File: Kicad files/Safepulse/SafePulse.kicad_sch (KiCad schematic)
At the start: 87 parts, among them IC1 S-35770E01I-K8T2U, J1 Conn_01x03_Male, J2 4208, Q1 FQT7N10L, Q2 BC846A, Q3 MMBT3906, Q4 MMBT3906, U1 TS4061AILT-1.25, U2 74HC14, U3 TLV27L1DBVT, U33 MAX9910EXK+T, U4 CD14538BM

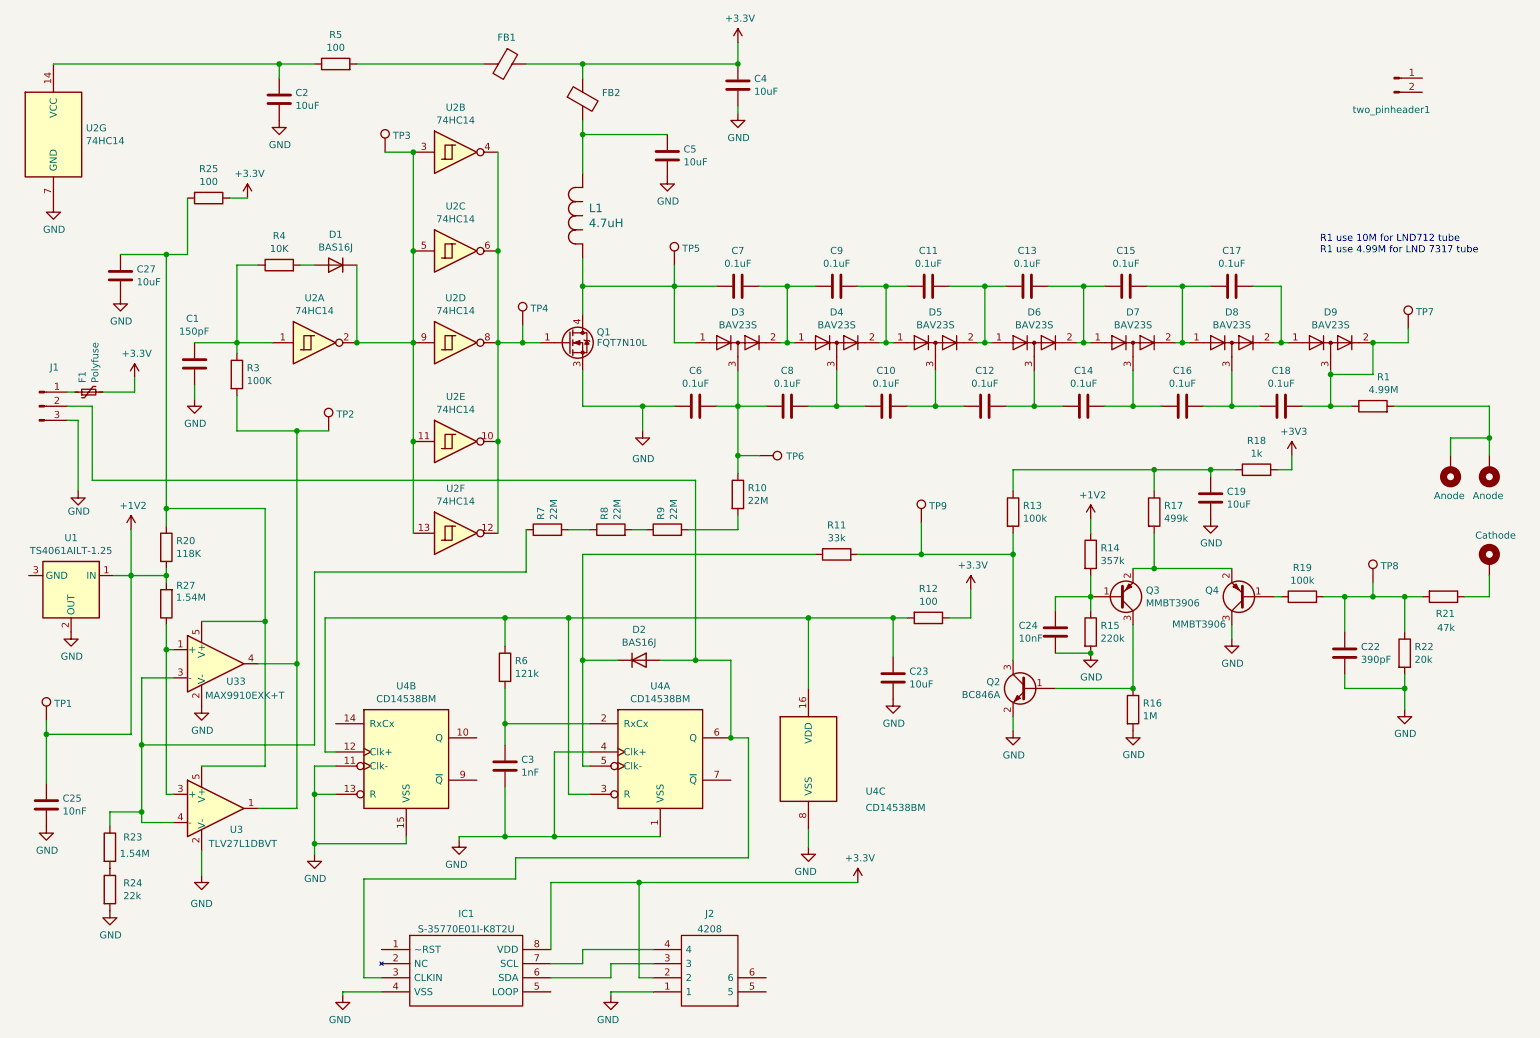
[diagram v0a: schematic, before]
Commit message: Updated C22 and R22 according to Joseph tests
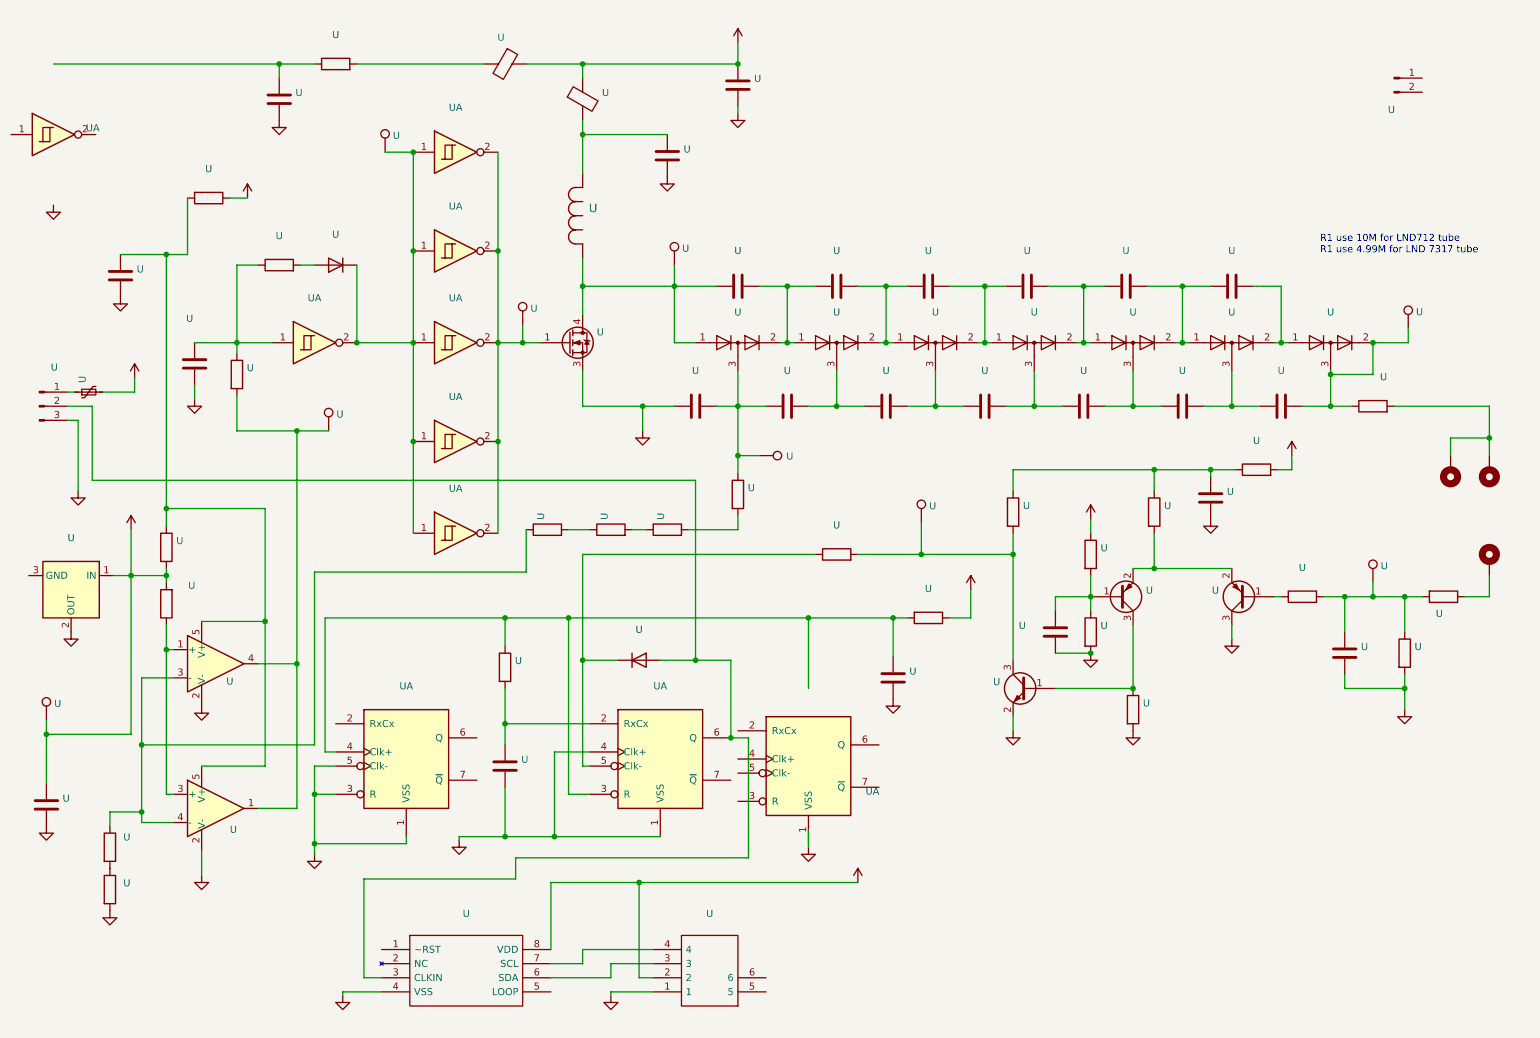
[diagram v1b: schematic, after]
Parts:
- U: renamed from U2; value 74HC14 -> (none); footprint Package_SO:SOIC-14_3.9x8.7mm_P1.27mm -> (none)
- U: renamed from D4; value BAV23S -> (none); footprint Package_TO_SOT_SMD:SOT-23 -> (none)
- U: renamed from D5; value BAV23S -> (none); footprint Package_TO_SOT_SMD:SOT-23 -> (none)
- U: renamed from D6; value BAV23S -> (none); footprint Package_TO_SOT_SMD:SOT-23 -> (none)
- U: renamed from D7; value BAV23S -> (none); footprint Package_TO_SOT_SMD:SOT-23 -> (none)
- U: renamed from D8; value BAV23S -> (none); footprint Package_TO_SOT_SMD:SOT-23 -> (none)
- U: renamed from D3; value BAV23S -> (none); footprint Package_TO_SOT_SMD:SOT-23 -> (none)
- U: renamed from D9; value BAV23S -> (none); footprint Package_TO_SOT_SMD:SOT-23 -> (none)
- U: renamed from C7; value 0.1uF -> (none); footprint Capacitor_SMD:C_0805_2012Metric -> (none)
- U: renamed from L1; value 4.7uH -> (none); footprint Inductor_SMD:L_Taiyo-Yuden_MD-4040 -> (none)
- U: renamed from R6; value 121k -> (none); footprint Resistor_SMD:R_0805_2012Metric -> (none)
- U: renamed from C5; value 10uF -> (none); footprint Capacitor_SMD:C_0805_2012Metric -> (none)
- U: renamed from R10; value 22M -> (none); footprint Resistor_SMD:R_0805_2012Metric -> (none)
- U: renamed from R9; value 22M -> (none); footprint Resistor_SMD:R_0805_2012Metric -> (none)
- U: renamed from R8; value 22M -> (none); footprint Resistor_SMD:R_0805_2012Metric -> (none)
- U: renamed from R7; value 22M -> (none); footprint Resistor_SMD:R_0805_2012Metric -> (none)
- U: renamed from R23; value 1.54M -> (none); footprint Resistor_SMD:R_0805_2012Metric -> (none)
- U: renamed from U4; value CD14538BM -> (none); footprint Package_SO:SOIC-16_3.9x9.9mm_P1.27mm -> (none)
- U: renamed from C3; value 1nF -> (none); footprint Capacitor_SMD:C_0805_2012Metric -> (none)
- U: renamed from FB1; value 74279220321 -> (none); footprint Resistor_SMD:R_0805_2012Metric -> (none)
- U: renamed from D2; value BAS16J -> (none); footprint Diode_SMD:D_SOD-323 -> (none)
- U: renamed from U1; value TS4061AILT-1.25 -> (none); footprint Package_TO_SOT_SMD:SOT-23 -> (none)
- U: renamed from R5; value 100 -> (none); footprint Resistor_SMD:R_0805_2012Metric -> (none)
- U: renamed from C2; value 10uF -> (none); footprint Capacitor_SMD:C_0805_2012Metric -> (none)
- U: renamed from R12; value 100 -> (none); footprint Resistor_SMD:R_0805_2012Metric -> (none)
- U: renamed from R20; value 118K -> (none); footprint Resistor_SMD:R_0805_2012Metric -> (none)
- U: renamed from C23; value 10uF -> (none); footprint Capacitor_SMD:C_0805_2012Metric -> (none)
- U: renamed from R3; value 100K -> (none); footprint Resistor_SMD:R_0805_2012Metric -> (none)
- U: renamed from D1; value BAS16J -> (none); footprint Diode_SMD:D_SOD-323 -> (none)
- U: renamed from R4; value 10K -> (none); footprint Resistor_SMD:R_0805_2012Metric -> (none)
- U: renamed from C1; value 150pF -> (none); footprint Capacitor_SMD:C_0805_2012Metric -> (none)
- U: renamed from R1; value 4.99M -> (none); footprint Resistor_SMD:R_1206_3216Metric -> (none)
- U: renamed from Q2; value BC846A -> (none); footprint Package_TO_SOT_SMD:SOT-23 -> (none)
- U: renamed from R11; value 33k -> (none); footprint Resistor_SMD:R_0805_2012Metric -> (none)
- U: renamed from C17; value 0.1uF -> (none); footprint Capacitor_SMD:C_0805_2012Metric -> (none)
- U: renamed from C19; value 10uF -> (none); footprint Capacitor_SMD:C_0805_2012Metric -> (none)
- U: renamed from J2; value 4208 -> (none); footprint 4208 -> (none)
- U: renamed from Q1; value FQT7N10L -> (none); footprint Package_TO_SOT_SMD:SOT-223-3_TabPin4 -> (none)
- U: renamed from C14; value 0.1uF -> (none); footprint Capacitor_SMD:C_0805_2012Metric -> (none)
- U: renamed from R13; value 100k -> (none); footprint Resistor_SMD:R_0805_2012Metric -> (none)
- U: renamed from TP2; value TestPoint -> (none); footprint TestPoint:TestPoint_Pad_1.0x1.0mm -> (none)
- U: renamed from C18; value 0.1uF -> (none); footprint Capacitor_SMD:C_0805_2012Metric -> (none)
- U: renamed from C9; value 0.1uF -> (none); footprint Capacitor_SMD:C_0805_2012Metric -> (none)
- U: renamed from H4; value Anode -> (none); footprint TestPoint:TestPoint_Loop_D3.50mm_Drill1.4mm_Beaded -> (none)
- U: renamed from C11; value 0.1uF -> (none); footprint Capacitor_SMD:C_0805_2012Metric -> (none)
- U: renamed from two_pinheader1; value Conn_01x03_Male -> (none); footprint Connector_PinHeader_2.54mm:PinHeader_1x02_P2.54mm_Vertical -> (none)
- U: renamed from TP5; value TestPoint -> (none); footprint TestPoint:TestPoint_Pad_1.0x1.0mm -> (none)
- U: renamed from C27; value 10uF -> (none); footprint Capacitor_SMD:C_0805_2012Metric -> (none)
- U: renamed from U33; value MAX9910EXK+T -> (none); footprint Package_TO_SOT_SMD:SOT-353_SC-70-5 -> (none)
- U: renamed from C25; value 10nF -> (none); footprint Capacitor_SMD:C_0805_2012Metric -> (none)
- U: renamed from TP8; value TestPoint -> (none); footprint TestPoint:TestPoint_Pad_1.0x1.0mm -> (none)
- U: renamed from C8; value 0.1uF -> (none); footprint Capacitor_SMD:C_0805_2012Metric -> (none)
- U: renamed from H1; value Cathode -> (none); footprint TestPoint:TestPoint_Loop_D2.60mm_Drill1.4mm_Beaded -> (none)
- U: renamed from C6; value 0.1uF -> (none); footprint Capacitor_SMD:C_0805_2012Metric -> (none)
- U: renamed from F1; value Polyfuse -> (none); footprint Resistor_SMD:R_0805_2012Metric -> (none)
- U: renamed from Q4; value MMBT3906 -> (none); footprint Package_TO_SOT_SMD:SOT-23 -> (none)
- U: renamed from R25; value 100 -> (none); footprint Resistor_SMD:R_0805_2012Metric -> (none)
- U: renamed from R21; value 47k -> (none); footprint Resistor_SMD:R_0805_2012Metric -> (none)
- U: renamed from R15; value 220k -> (none); footprint Resistor_SMD:R_0805_2012Metric -> (none)
- U: renamed from TP4; value TestPoint -> (none); footprint TestPoint:TestPoint_Pad_1.0x1.0mm -> (none)
- U: renamed from C16; value 0.1uF -> (none); footprint Capacitor_SMD:C_0805_2012Metric -> (none)
- U: renamed from C22; value 390pF -> (none); footprint Capacitor_SMD:C_0805_2012Metric -> (none)
- U: renamed from C15; value 0.1uF -> (none); footprint Capacitor_SMD:C_0805_2012Metric -> (none)
- U: renamed from R19; value 100k -> (none); footprint Resistor_SMD:R_0805_2012Metric -> (none)
- U: renamed from C24; value 10nF -> (none); footprint Capacitor_SMD:C_0805_2012Metric -> (none)
- U: renamed from TP9; value TestPoint -> (none); footprint TestPoint:TestPoint_Pad_1.0x1.0mm -> (none)
- U: renamed from TP7; value TestPoint -> (none); footprint TestPoint:TestPoint_Pad_1.0x1.0mm -> (none)
- U: renamed from TP3; value TestPoint -> (none); footprint TestPoint:TestPoint_Pad_1.0x1.0mm -> (none)
- U: renamed from H2; value Anode -> (none); footprint TestPoint:TestPoint_Loop_D3.50mm_Drill1.4mm_Beaded -> (none)
- U: renamed from C4; value 10uF -> (none); footprint Capacitor_SMD:C_0805_2012Metric -> (none)
- U: renamed from R24; value 22k -> (none); footprint Resistor_SMD:R_0805_2012Metric -> (none)
- U: renamed from U3; value TLV27L1DBVT -> (none); footprint Package_TO_SOT_SMD:SOT-23-5 -> (none)
- U: renamed from R16; value 1M -> (none); footprint Resistor_SMD:R_0805_2012Metric -> (none)
- U: renamed from TP1; value TestPoint -> (none); footprint TestPoint:TestPoint_Pad_1.0x1.0mm -> (none)
- U: renamed from C10; value 0.1uF -> (none); footprint Capacitor_SMD:C_0805_2012Metric -> (none)
- U: renamed from IC1; value S-35770E01I-K8T2U -> (none); footprint SOP65P400X80-8N -> (none)
- U: renamed from R14; value 357k -> (none); footprint Resistor_SMD:R_0805_2012Metric -> (none)
- U: renamed from Q3; value MMBT3906 -> (none); footprint Package_TO_SOT_SMD:SOT-23 -> (none)
- U: renamed from C13; value 0.1uF -> (none); footprint Capacitor_SMD:C_0805_2012Metric -> (none)
- U: renamed from R18; value 1k -> (none); footprint Resistor_SMD:R_0805_2012Metric -> (none)
- U: renamed from FB2; value 74279220321 -> (none); footprint Resistor_SMD:R_0805_2012Metric -> (none)
- U: renamed from J1; value Conn_01x03_Male -> (none); footprint Connector_PinHeader_2.54mm:PinHeader_1x03_P2.54mm_Vertical -> (none)
- U: renamed from C12; value 0.1uF -> (none); footprint Capacitor_SMD:C_0805_2012Metric -> (none)
- U: renamed from R17; value 499k -> (none); footprint Resistor_SMD:R_0805_2012Metric -> (none)
- U: renamed from R22; value 20k -> (none); footprint Resistor_SMD:R_0805_2012Metric -> (none)
- U: renamed from TP6; value TestPoint -> (none); footprint TestPoint:TestPoint_Pad_1.0x1.0mm -> (none)
- U: renamed from R27; value 1.54M -> (none); footprint Resistor_SMD:R_0805_2012Metric -> (none)
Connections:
- net GND: now also U.1 (VSS), U.3 (R), U.5 (Clk-); no longer U.11 (Clk-), U.13 (R), U.15 (VSS), U.7 (GND), U.8 (VSS)
- net at U.1, U.1: no longer U.14 (VCC)
- net at U.1, U.1, U.2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: now also U.4 (Clk+); no longer U.12 (Clk+), U.16 (VDD)
- new net: U.1, U.1, U.1, U.1, U.1, U.1, U.1 (K), U.2
- new net: U.1, U.1 (G), U.2, U.2, U.2, U.2, U.2
